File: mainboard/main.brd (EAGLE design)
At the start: 48.3 x 45.7 mm, 4 parts, among them J1 501645-2620, J2 RJHSE-3380, J3 RJHSE-3380

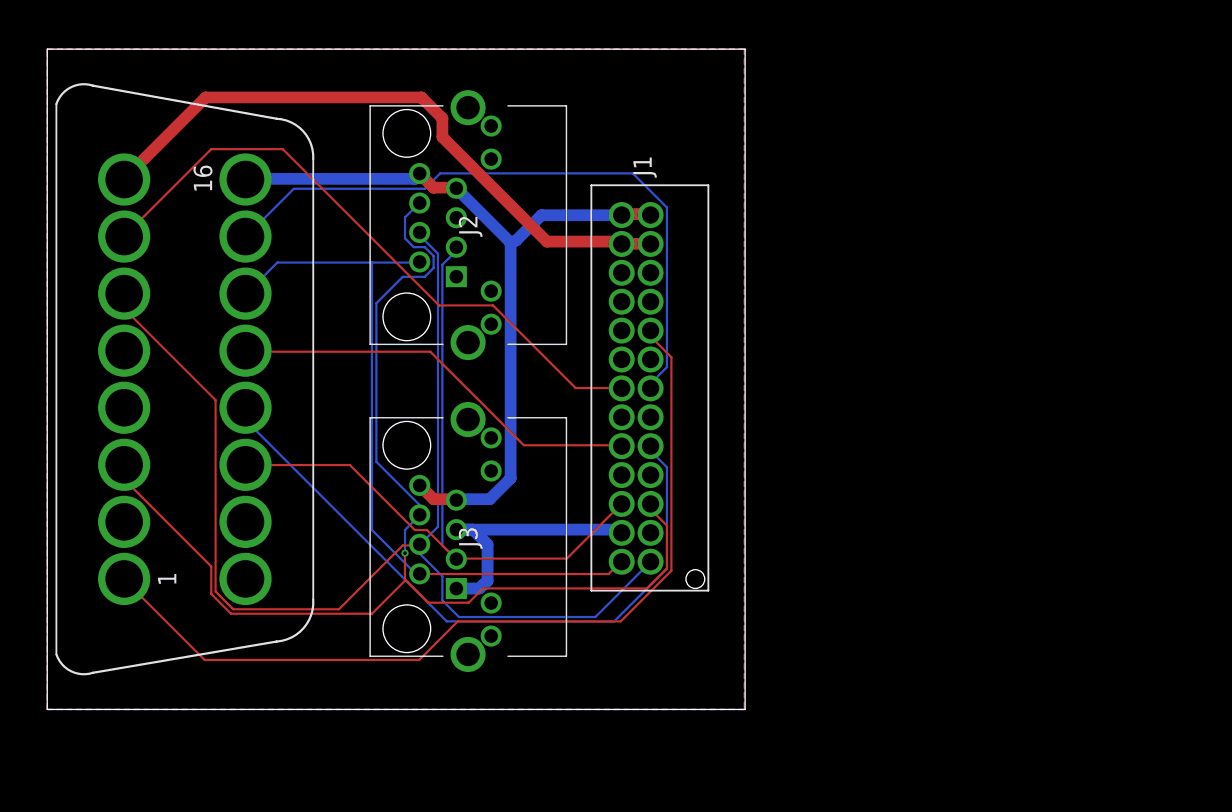
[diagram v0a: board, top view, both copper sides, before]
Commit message: switch to rj45 for the interconnect
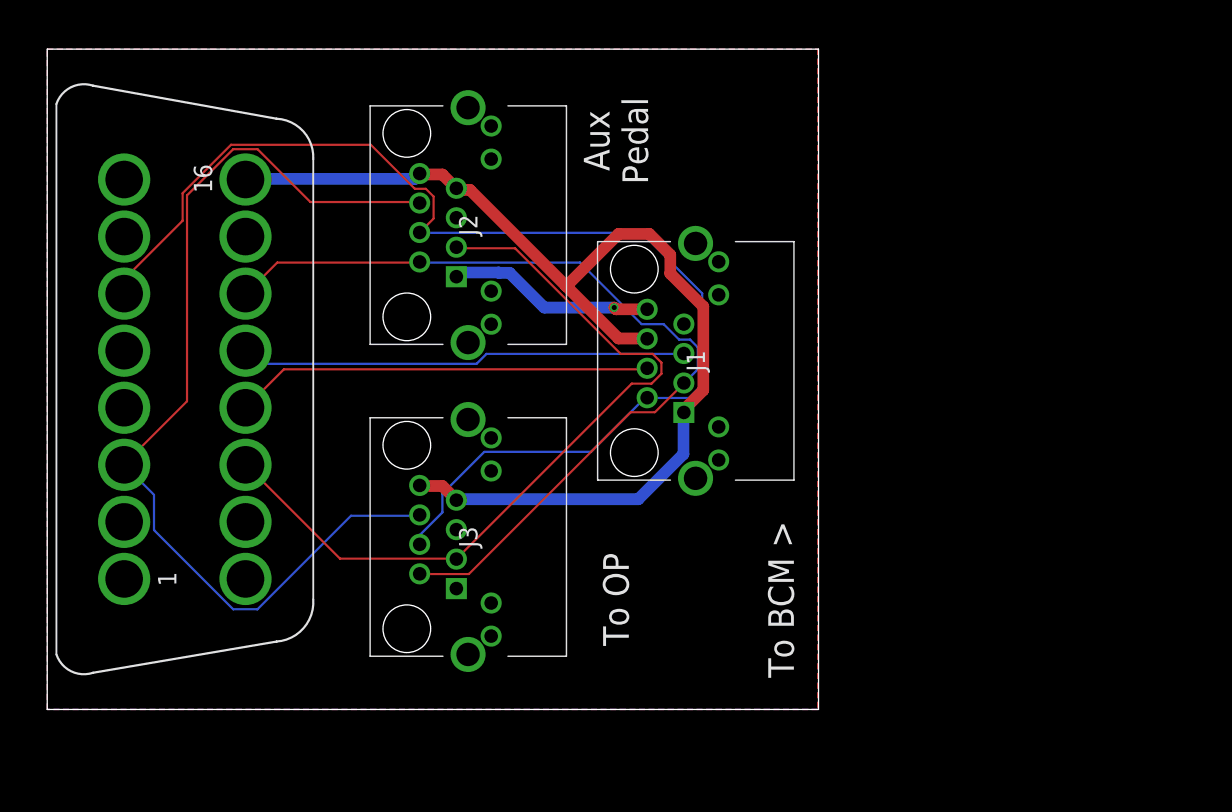
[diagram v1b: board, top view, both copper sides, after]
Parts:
- J1: value 501645-2620 -> RJHSE-3380; device Souers:501645-2620 -> RJHSE-3380:RJHSE3384
- moved J1 6.65 mm to (38.1, 24.1), turned to 270 degrees
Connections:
- removed net AUX2: J1.17
- removed net AUX3: J1.20
- removed net AUX4: J1.19
- net CAN0_L: now also J1.3; no longer J1.1
- net CAN1_H: no longer J1.6
- net CAN1_L: no longer J1.5
- net CAN2_H: now also J1.4; no longer J1.10
- net CAN2_L: now also J1.5; no longer J1.9
- net GMLAN: no longer J1.18
- net GND: no longer J1.11, J1.12, J1.15, J1.16, J1.21, J1.22, J1.3, J1.4
- net IGN: no longer J1.23, J1.24
- net K_LINE: no longer J1.13
- net L_LINE: no longer J1.14
- net VIN: now also J1.1, J1.6; no longer J1.25, J1.26
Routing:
- net GMLAN: track 60.0 -> 0.00 mm
- net L_LINE: track 45.0 -> 0.00 mm
- net K_LINE: track 43.8 -> 0.00 mm
- net IGN: track 43.7 -> 0.00 mm
- net VIN: track 54.8 -> 77.4 mm
- net CAN2_H: track 46.3 -> 29.0 mm
- net CAN1_H: track 83.1 -> 68.2 mm, vias 1 -> 0
- net CAN0_L: track 50.4 -> 61.3 mm
- net GND: track 19.0 -> 14.4 mm, vias 0 -> 1
- net CAN1_L: track 52.7 -> 55.1 mm
- net CAN2_L: track 28.8 -> 31.0 mm
- net CAN0_H: track 83.4 -> 84.7 mm
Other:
- board size 48.3 x 45.7 mm -> 53.4 x 45.7 mm
- board text added: "Aux Pedal"
- board text added: "To BCM >"
- board text added: "To OP"

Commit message: push
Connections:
- net CAN0_H: now also J2.6, J3.6; no longer J1.2, J2.4, J3.4
- net CAN0_L: now also J2.3, J3.3; no longer J1.3, J2.2, J3.2
- net CAN1_H: now also J1.4; no longer J2.6, J3.6
- net CAN1_L: now also J1.5; no longer J2.3, J3.3
- net CAN2_H: now also J1.2, J2.4, J3.4; no longer J1.4
- net CAN2_L: now also J1.3, J2.2, J3.2; no longer J1.5
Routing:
- net CAN2_L: track 31.0 -> 65.2 mm
- net CAN0_H: track 84.7 -> 52.7 mm, vias 0 -> 1
- net CAN2_H: track 29.0 -> 54.2 mm
- net CAN0_L: track 61.3 -> 37.1 mm
- net CAN1_L: track 55.1 -> 33.5 mm
- net CAN1_H: track 68.2 -> 48.7 mm
- net VIN: track 77.4 -> 59.9 mm, vias 0 -> 1
- net GND: track 14.4 -> 0.00 mm, vias 1 -> 0
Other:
- board text added: "^To OP"
- board text added: "^To Pedal or AUX"
- board text removed: "Aux Pedal"
- board text removed: "To OP"

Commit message: main v2
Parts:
- removed J1, J2, J3: RJHSE-3380, RJHSE-3380:RJHSE3384
- added C2, CPV2, LEGACY: RA-RJ45RA, comma.ai:RA-RJ45
- added OPTION: 34793-0041, 34793-0041:347930041
- moved PANDA 29.0 mm to (38.1, 27.9), turned to 180 degrees
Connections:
- net CAN0_H: now also C2.6, CPV2.6, LEGACY.6; no longer J2.6, J3.6
- net CAN0_L: now also C2.3, CPV2.3, LEGACY.3; no longer J2.3, J3.3
- net CAN1_H: now also OPTION.1, OPTION.3; no longer J1.4
- net CAN1_L: now also OPTION.2, OPTION.4; no longer J1.5
- net CAN2_H: now also C2.4, CPV2.4; no longer J1.2, J2.4, J3.4
- net CAN2_L: now also C2.2, CPV2.2; no longer J1.3, J2.2, J3.2
- net GND: now also C2.1, C2.5, C2.P$1, C2.P$2, CPV2.1, CPV2.5, CPV2.P$1, CPV2.P$2, LEGACY.1, LEGACY.5, LEGACY.P$1, LEGACY.P$2; no longer J1.7, J1.8, J2.1, J2.5, J3.1, J3.5
- net VIN: now also C2.7, C2.8, CPV2.7, CPV2.8, LEGACY.2; no longer J1.1, J1.6, J2.7, J2.8, J3.7, J3.8
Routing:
- net GND: track 0.00 -> 247.7 mm, vias 0 -> 6
- net CAN0_H: track 52.7 -> 95.3 mm
- net CAN0_L: track 37.1 -> 69.8 mm, vias 0 -> 1
- net CAN2_L: track 65.2 -> 38.6 mm
- net VIN: track 59.9 -> 82.7 mm, vias 1 -> 0
- net CAN2_H: track 54.2 -> 33.7 mm
- net CAN1_L: track 33.5 -> 26.0 mm, vias 0 -> 1
- net CAN1_H: track 48.7 -> 48.0 mm
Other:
- board size 53.4 x 45.7 mm -> 76.3 x 39.4 mm
- board text added: "JLCJLCJLCJLC"
- board text added: "body harness - main"
- board text added: "csouers 8/18/2020"
- board text added: "github.com/csouers"
- board text removed: "To BCM >"
- board text removed: "^To OP"
- board text removed: "^To Pedal or AUX"
- board text removed: "body harness - main board"
- board text removed: "csouers 7/1/2020"
- board text removed: "github.com/csouers/bodyharness"
